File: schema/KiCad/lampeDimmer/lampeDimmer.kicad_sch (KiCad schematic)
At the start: 24 parts, among them J1 PICkit4, J2 USART, J3 EXT_IO, J4 EXT_PWM4B, J5 EXT_PWM4D, J6 EXT_ADC1, J7 CON_POT_SW, J8 Entrée, J9 Sortie, M1 ARDUINO_MICRO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

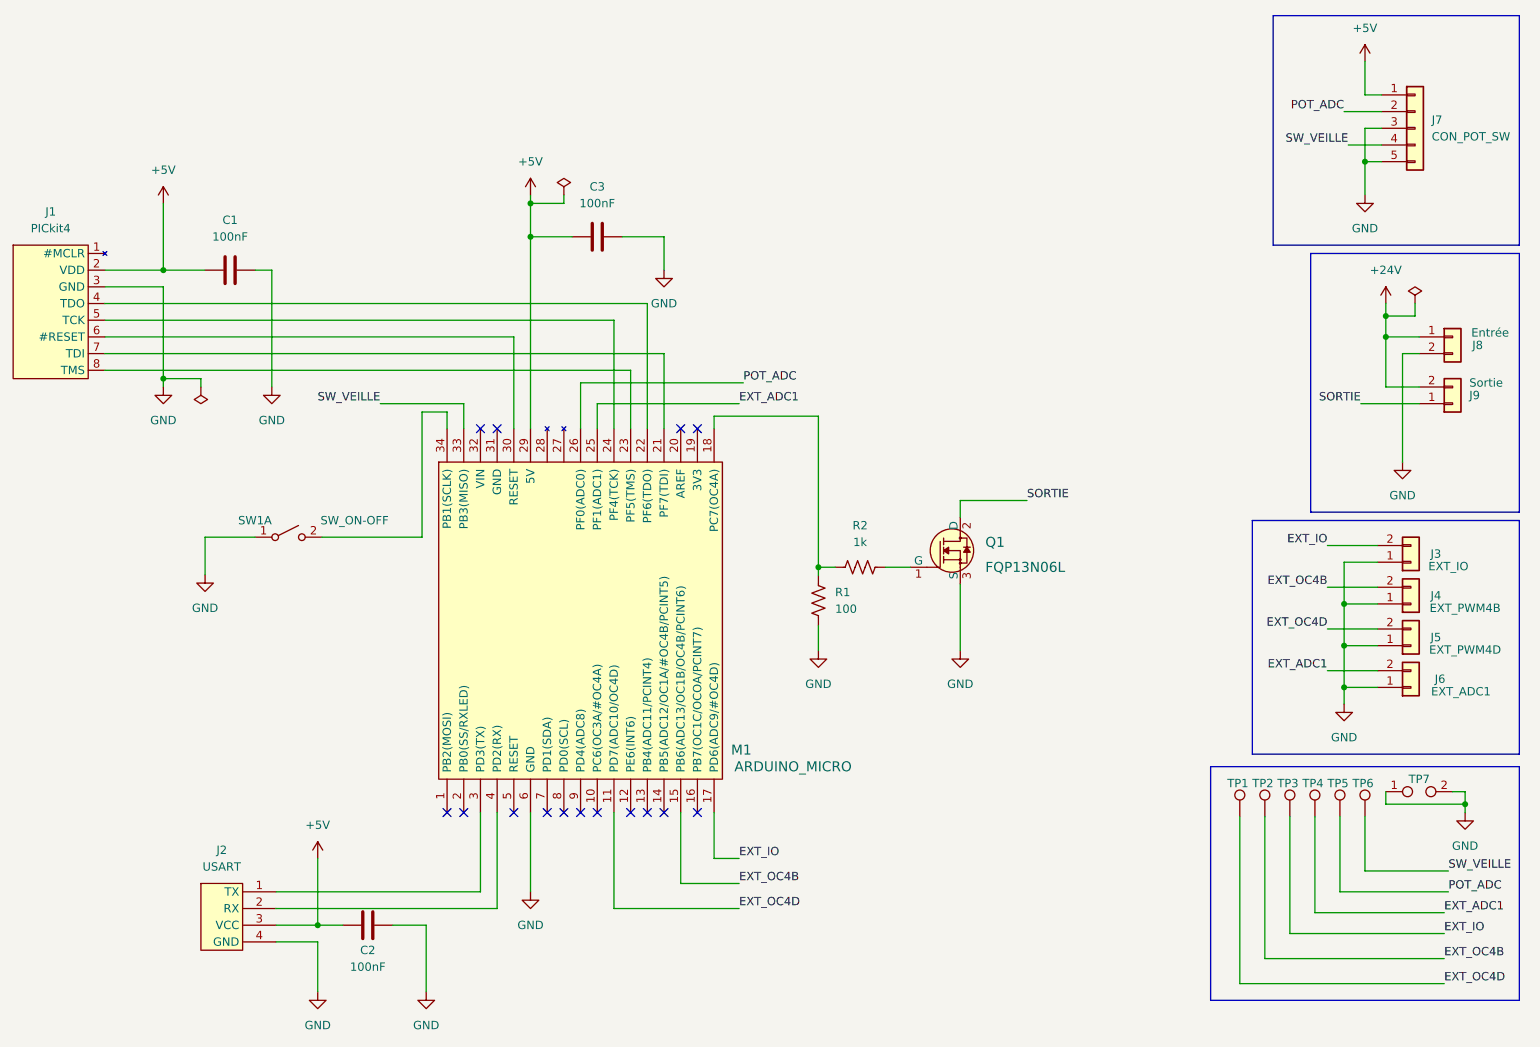
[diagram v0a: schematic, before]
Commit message: ~ Mise à jours des noms de labels sur le schéma. ~ Mise à jours du PCB. ~ Mise à jours des fichiers Gerbers.
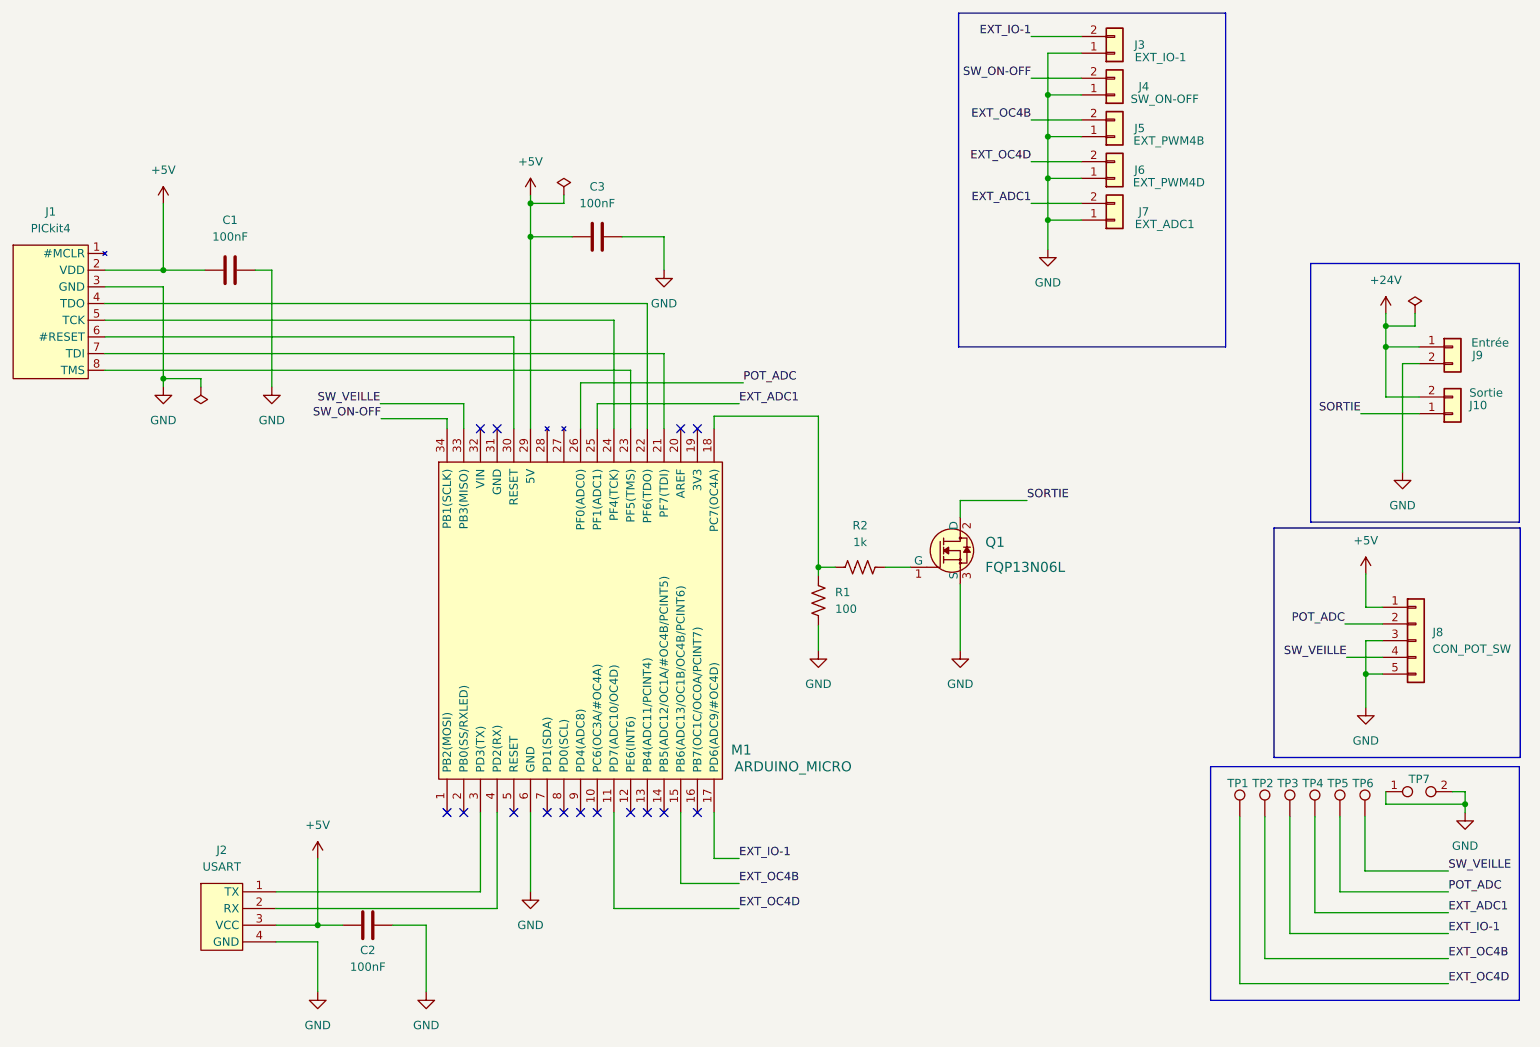
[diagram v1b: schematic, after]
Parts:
- removed SW1: SW_ON-OFF, Connector_PinSocket_2.54mm:PinSocket_1x02_P2.54mm_Vertical, symbol Switch:SW_DPST_x2
- added J4: SW_ON-OFF, Connector_PinSocket_2.54mm:PinSocket_1x02_P2.54mm_Vertical, symbol Connector_Generic:Conn_01x02
- J3: value EXT_IO -> EXT_IO-1
- renumbered J9 to J10, J4 to J5, J5 to J6, J6 to J7, J7 to J8, J8 to J9
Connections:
- net GND: now also J4.1 (Pin_1)
- net SW_ON-OFF: now reaches M1.34 (PB1(SCLK))
- net SW_ON-OFF: now also J4.2 (Pin_2)
- net EXT_IO renamed EXT_IO-1
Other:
- moved on the sheet: J10, J3, J5, J6, J7, J8, J9
